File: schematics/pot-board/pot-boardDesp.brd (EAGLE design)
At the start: 86.4 x 41.9 mm, 15 parts, among them J3 POWER_JACKPTH_LOCK, U1 SPARKFUN_PRO_MICRO, U2 DC-DC-STEP-DOWN-LM2596

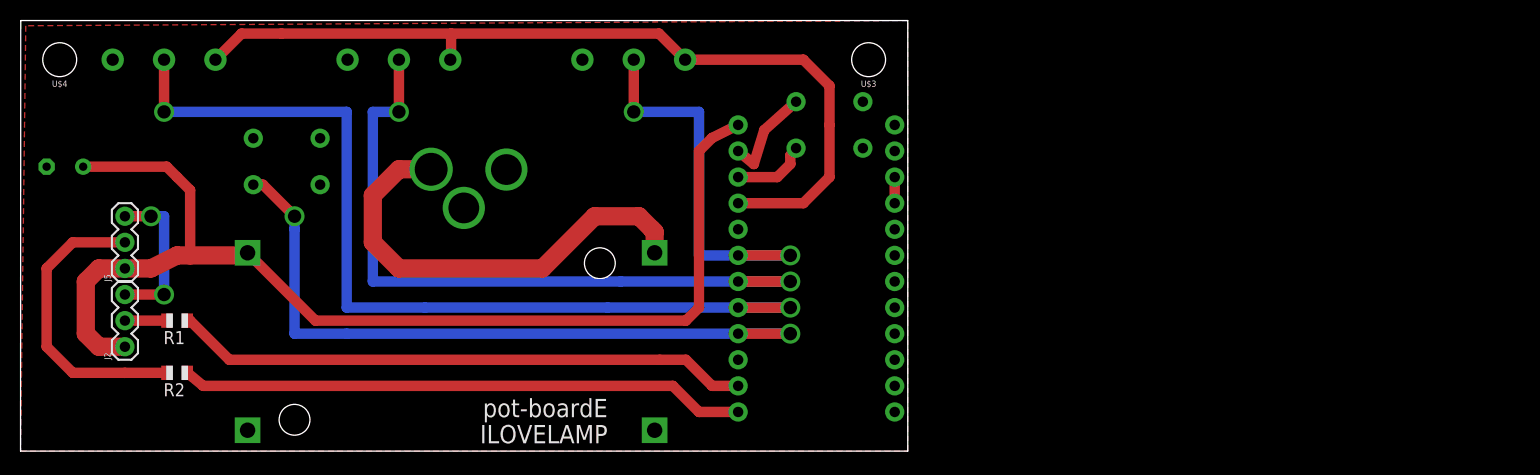
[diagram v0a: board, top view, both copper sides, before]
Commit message: added esp pot boards
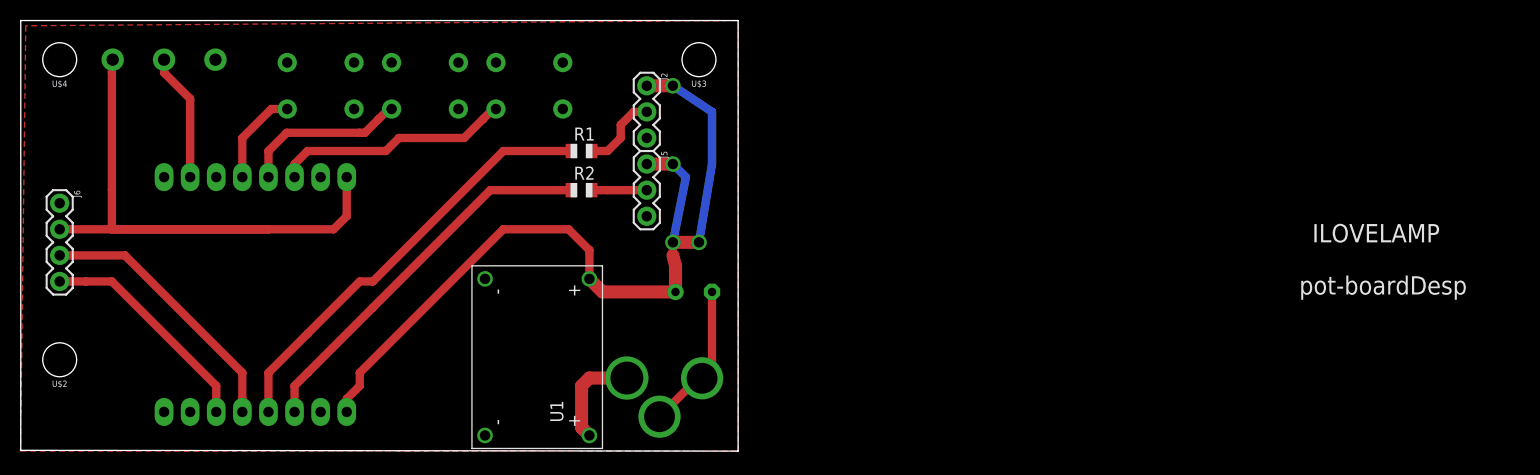
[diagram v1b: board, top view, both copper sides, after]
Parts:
- removed R4, R5: (no value), pot:3RP/1610N
- removed S4: tact6mm, SparkFun-Switches:TACTILE_SWITCH_PTH_6.0MM
- removed U2: DC-DC-STEP-DOWN-LM2596, diy-modules:DC-DC-STEP-DOWN-LM2596
- added J6: (no value), SparkFun-Connectors:1X04
- added S2, S3: tact6mm, SparkFun-Switches:TACTILE_SWITCH_PTH_6.0MM
- added U$2: (no value), SparkFun-Hardware:STAND-OFF
- added WEMOS1: (no value), esp8266modules:WEMOS-D1-MINI
- U1: value SPARKFUN_PRO_MICRO -> MH-MINI-360MINI-360; device SparkFun-Boards:SPARKFUN_PRO_MICRO -> MP1584EN-1484249208697-powermodules:MH-MINI-360
- moved C2 62.4 mm to (65.5, 15.5), turned to 180 degrees
- moved J2 56.8 mm to (61.0, 35.6), turned to 270 degrees
- moved J5 51.8 mm to (61.0, 27.9), turned to 270 degrees
- moved R2 43.2 mm to (54.6, 25.4), turned to 0 degrees
- moved R1 42.7 mm to (54.6, 29.2), turned to 0 degrees
- moved U1 28.9 mm to (50.3, 9.14), flipped to the top, turned to 90 degrees
- moved J3 27.9 mm to (72.9, 7.11)
- moved U$3 16.5 mm to (66.0, 38.1)
- moved S1 8.07 mm to (29.2, 35.6)
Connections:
- removed net A1: R4.2, U1.18
- removed net A2: R5.2, U1.19
- removed net N$5: U1.12
- removed net N$6: U1.15
- removed net RESET: S4.1, U1.22
- removed net RR: U1.7
- removed net VCC: R3.3, R4.3, R5.3, U1.21
- new net +3V3: J6.2, R3.1, WEMOS1.3V3
- new net BUTT2: S2.1, WEMOS1.D6
- new net BUTT3: S3.1, WEMOS1.D7
- net A0: now also WEMOS1.A0; no longer U1.17
- net BUTT1: now also WEMOS1.D5; no longer U1.16
- net GND: now also J6.1, R3.3, S2.3, S3.3, U1.P$1, U1.P$4, WEMOS1.GND; no longer R3.1, R4.1, R5.1, S4.3, U1.23, U1.3, U1.4, U2.IN-, U2.OUT-
- net LED1: now also WEMOS1.D4; no longer U1.13
- net LED2: now also WEMOS1.D3; no longer U1.14
- net N$1: now also U1.P$2; no longer U2.IN+
- net SCL: now also J6.4, WEMOS1.D1; no longer U1.6
- net SDA: now also J6.3, WEMOS1.D2; no longer U1.5
- net VIN: now also U1.P$3, WEMOS1.5V; no longer U1.24, U2.OUT+
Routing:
- net VCC: track 84.4 -> 0.00 mm
- net A0: track 90.2 -> 12.5 mm, vias 2 -> 0
- net A1: track 69.9 -> 0.00 mm, vias 2 -> 0
- net +3V3: track 0.00 -> 64.0 mm
- net BUTT1: track 70.1 -> 9.35 mm, vias 2 -> 0
- net A2: track 39.4 -> 0.00 mm, vias 2 -> 0
- net N$1: track 44.6 -> 9.87 mm
- net VIN: track 113.7 -> 85.7 mm, vias 0 -> 4
- net SDA: track 0.00 -> 26.3 mm
- net LED1O: track 29.0 -> 5.35 mm
- net BUTT3: track 0.00 -> 23.1 mm
- net SCL: track 0.00 -> 22.0 mm
- net LED1: track 55.1 -> 37.4 mm
- net BUTT2: track 0.00 -> 16.2 mm
- net LED2: track 56.2 -> 42.2 mm
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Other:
- board size 86.4 x 41.9 mm -> 69.8 x 41.9 mm
- board text added: "pot-boardDesp"
- board text removed: "pot-boardE"
